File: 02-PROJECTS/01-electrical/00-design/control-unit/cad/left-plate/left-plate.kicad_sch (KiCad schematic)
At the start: 16 parts, among them J1 plate cable header 2x6 shroud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, SW1 key - hatch, SW2 key - fuel door, U1 IS31FL3218-QFLS2-TR

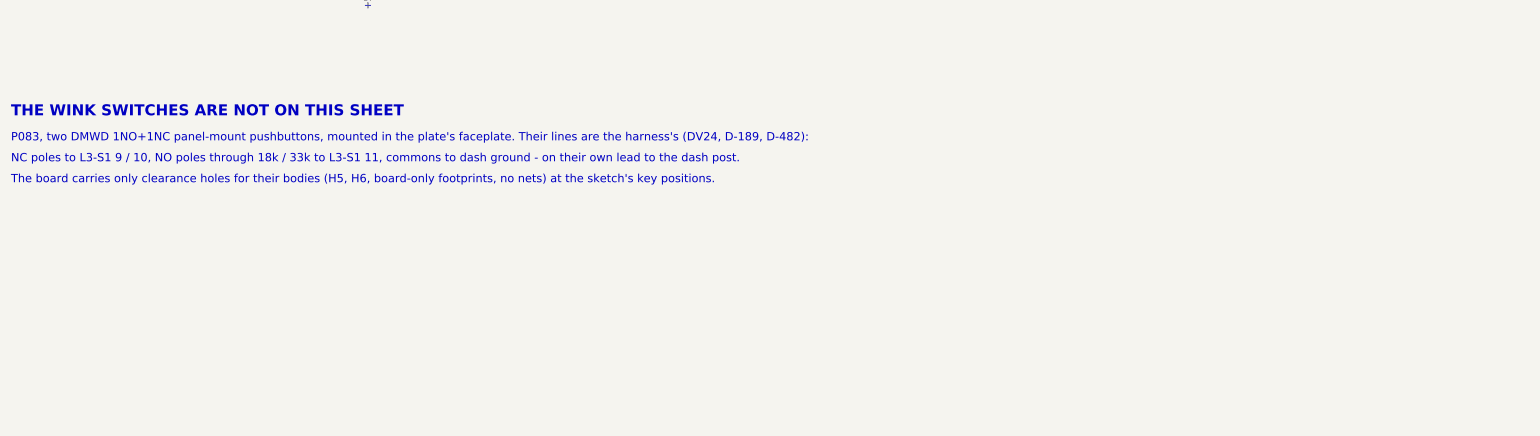
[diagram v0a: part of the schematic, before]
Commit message: Electrical: the left plate regenerated - P204 winks on the board at 19 mm, the wink lead on J2, the wink check in check.py (D-499, D-504)
Y22 done. ERC 0, DRC 0/0/0, check.py 29 checks 0 mismatches on the plate with check_winks (J2 against the L3-S1 rows that land on it, resistor values from cavity 11); the other boards unchanged. P204's footprint, J2's housing and run and R3/R4's part numbers confirm. The design README's plate row follows in the next commit with the export section.

Co-Authored-By: Claude Fable 5.1 <noreply@anthropic.com>
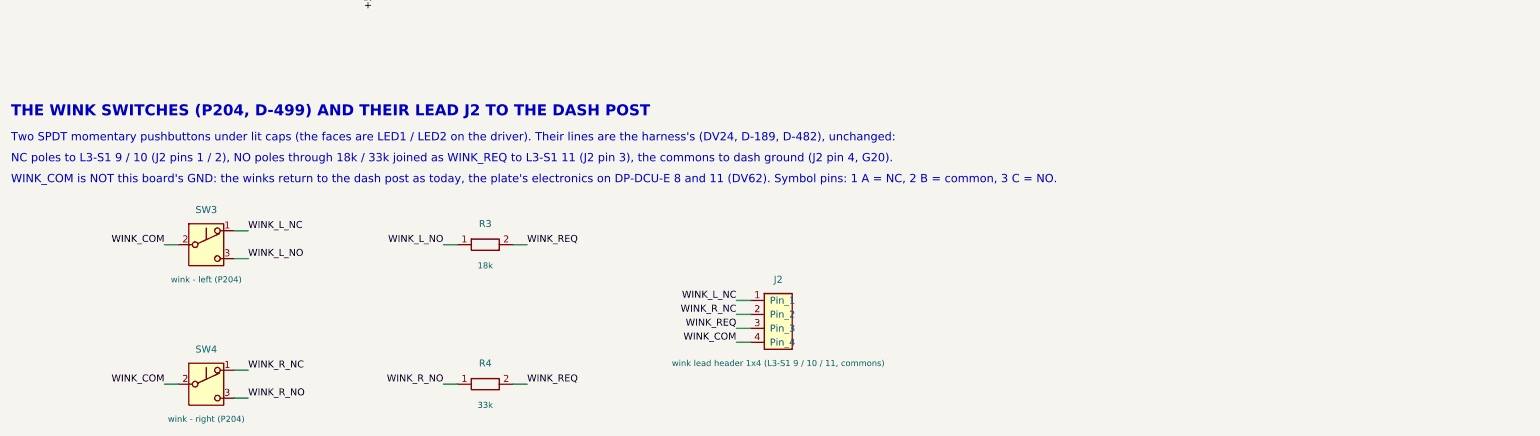
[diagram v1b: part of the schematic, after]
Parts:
- added J2: wink lead header 1x4 (L3-S1 9 / 10 / 11, commons), Connector_JST:JST_XH_B4B-XH-A_1x04_P2.50mm_Vertical, symbol left-plate:Conn_01x04
- added R3: 18k, Resistor_SMD:R_0603_1608Metric, symbol left-plate:R
- added R4: 33k, Resistor_SMD:R_0603_1608Metric, symbol left-plate:R
- added SW3: wink - left (P204), left-plate:WinkSwitch_P204_SPDT_Placeholder, symbol left-plate:SW_Push_SPDT
- added SW4: wink - right (P204), left-plate:WinkSwitch_P204_SPDT_Placeholder, symbol left-plate:SW_Push_SPDT
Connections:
- new net WINK_COM: J2.4 (Pin_4), SW3.2 (B), SW4.2 (B)
- new net WINK_L_NC: J2.1 (Pin_1), SW3.1 (A)
- new net WINK_L_NO: R3.1, SW3.3 (C)
- new net WINK_REQ: J2.3 (Pin_3), R3.2, R4.2
- new net WINK_R_NC: J2.2 (Pin_2), SW4.1 (A)
- new net WINK_R_NO: R4.1, SW4.3 (C)
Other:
- note added: "NC poles to L3-S1 9 / 10 (J2 pins 1 / 2), NO poles through 18k / 33k joined as WINK_REQ to L3-S1 11 (J2 pin 3), the commons to dash ground (J2 pin 4, G20)."
- note added: "THE WINK SWITCHES (P204, D-499) AND THEIR LEAD J2 TO THE DASH POST"
- note added: "Two SPDT momentary pushbuttons under lit caps (the faces are LED1 / LED2 on the driver). Their lines are the harness's (DV24, D-189, D-482), unchanged:"
- note added: "WINK_COM is NOT this board's GND: the winks return to the dash post as today, the plate's electronics on DP-DCU-E 8 and 11 (DV62). Symbol pins: 1 A = NC, 2 B = common, 3 C = NO."
- note removed: "NC poles to L3-S1 9 / 10, NO poles through 18k / 33k to L3-S1 11, commons to dash ground - on their own lead to the dash post."
- note removed: "P083, two DMWD 1NO+1NC panel-mount pushbuttons, mounted in the plate's faceplate. Their lines are the harness's (DV24, D-189, D-482):"
- note removed: "THE WINK SWITCHES ARE NOT ON THIS SHEET"
- note removed: "The board carries only clearance holes for their bodies (H5, H6, board-only footprints, no nets) at the sketch's key positions."
- title: Left plate - the panel's second face, left of the steering wheel (D-492) -> Left plate - the panel's second face, left of the steering wheel (D-492, D-499)

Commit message: Electrical: the CUR board takes the latching hazard button and the screen knob's header; its mock-up the knob (D-586, D-589, D-581)
Y62, Y50, Y51 (the CUR part). The plate board rev 0.03 from its generator: SW5 latching button with
R5 4.7 k and R6 47 k on a 5-way J2, LED6 the red triangle on OUT6 (the mirror symbol to OUT13, the
DCU's lights.h follows), J4 a STEMMA QT header for the knob's I2C board, the plate 118 x 56 (its
face's layout is block 01.60). ERC 0, DRC 0 with parity, check.py left-plate 31 / 0 with a new hazard
rule. The board script finishes leftovers with freerouting. The CUR mock-up's hazard opening and the
screen knob (24 / 24). The Digi-Key cart gains P219's board and lead.

Co-Authored-By: Claude Opus 5.5 <noreply@anthropic.com>
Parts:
- added J4: screen knob lead header (STEMMA QT, P219), Connector_JST:JST_SH_BM04B-SRSS-TB_1x04-1MP_P1.00mm_Vertical, symbol left-plate:Conn_01x04
- added LED6: LED 0603 - hazard red triangle (OUT6), LED_SMD:LED_0603_1608Metric, symbol left-plate:LED
- added R5: 4.7k, Resistor_SMD:R_0603_1608Metric, symbol left-plate:R
- added R6: 47k, Resistor_SMD:R_0603_1608Metric, symbol left-plate:R
- added SW5: hazard - latching (P226), left-plate:HazardSwitch_P226_Latching_Placeholder, symbol left-plate:SW_SPST
- J2: value wink lead header 1x4 (L3-S1 9 / 10 / 11, commons) -> wink lead header 1x5 (L3-S1 9 / 10 / 11, commons, L3-S1 6); footprint Connector_JST:JST_XH_B4B-XH-A_1x04_P2.50mm_Vertical -> Connector_JST:JST_XH_B5B-XH-A_1x05_P2.50mm_Vertical; symbol left-plate:Conn_01x04 -> left-plate:Conn_01x05; Confirm the wink lead's plate end (DV24, D-499): pin 1 = L3-S1 9, 2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 -> the wink lead's plate end (DV24, D-499, D-586): pin 1 = L3-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
- LED5: value LED 0603 - mirror stick symbol (OUT5) -> LED 0603 - mirror stick symbol (OUT13)
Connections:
- net +3V3: now also J4.2 (Pin_2)
- net +5V_PNL: now also LED6.2 (A)
- net GND: now also J4.1 (Pin_1)
- net LED_MIRROR: now also U1.19 (OUT13); no longer U1.11 (OUT5)
- net PNL_SCL: now also J4.4 (Pin_4)
- net PNL_SDA: now also J4.3 (Pin_3)
- net WINK_COM: now also R6.2, SW5.2 (B)
- net LED_HAZARD: now reaches U1.12 (OUT6)
- net LED_HAZARD: now also LED6.1 (K)
- new net HAZ_LADDER: J2.5 (Pin_5), R5.1, R6.1
- new net HAZ_SW: R5.2, SW5.1 (A)
- no-connect marks 13 -> 12
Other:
- note added: "Its red-triangle cap is LED6 on the driver's OUT6. The column's F-02 hazard contact is left unconnected (D-586)."
- note added: "J4 - THE SCREEN KNOB'S LEAD (P219, D-580, D-581)"
- note added: "L3-S1 6 (J2 pin 5) -> 4.7k -> the button -> the winks' commons (J2 pin 4, G20); 47k across the whole (D-368): the A8 ladder reads HAZARD while it is in."
- note added: "OUT1 wink L face, OUT2 wink R face, OUT3 hatch, OUT4 fuel door, OUT6 hazard, OUT13 mirror stick - the DCU firmware's map (lights.h, F-018, Y62)"
- note added: "OUT5, OUT7-OUT12, OUT14-OUT18 open. The bus pull-ups are on the carrier (R51 / R52, 4.7k to +3V3); none here."
- note added: "STEMMA QT order: 1 GND, 2 +3V3, 3 PNL_SDA, 4 PNL_SCL. The knob's encoder board (seesaw 0x36) stands off the plate's front, its shaft through the faceplate."
- note added: "THE HAZARD (P226, D-586, D-589): A LATCHING BUTTON ON THE WINK LEAD"
- note added: "WINK_COM is NOT this board's GND: the winks return to the dash post as today, the plate's electronics on DP-DCU 43 and 46 (DV62). Symbol pins: 1 A = NC, 2 B = common, 3 C = NO."
- note removed: "OUT1 wink L face, OUT2 wink R face, OUT3 hatch, OUT4 fuel door, OUT5 mirror stick - the DCU firmware's map (lights.h, F-018)"
- note removed: "OUT6-OUT18 open. The bus pull-ups are on the carrier (R51 / R52, 4.7k to +3V3); none here."
- note removed: "WINK_COM is NOT this board's GND: the winks return to the dash post as today, the plate's electronics on DP-DCU-E 8 and 11 (DV62). Symbol pins: 1 A = NC, 2 B = common, 3 C = NO."
